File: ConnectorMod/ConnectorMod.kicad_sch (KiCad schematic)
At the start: 82 parts, among them J1 PJ-325, J10 VIN, J11 VCC, J12 MRX, J13 MTX, J14 DACL, J15 DACR, J16 DACG, J17 VSW, J2 PJ-325, J3 PJ-325, J4 PJ-066A, J5 BAT1, J6 BAT2, J7 AMP, J8 GNDA, J9 GND, Q1 MMBT3904, Q2 MMBT3904, Q3 MMBT3906, U1 TLP2366, U2 74LVC1G08, U3 TLV2372

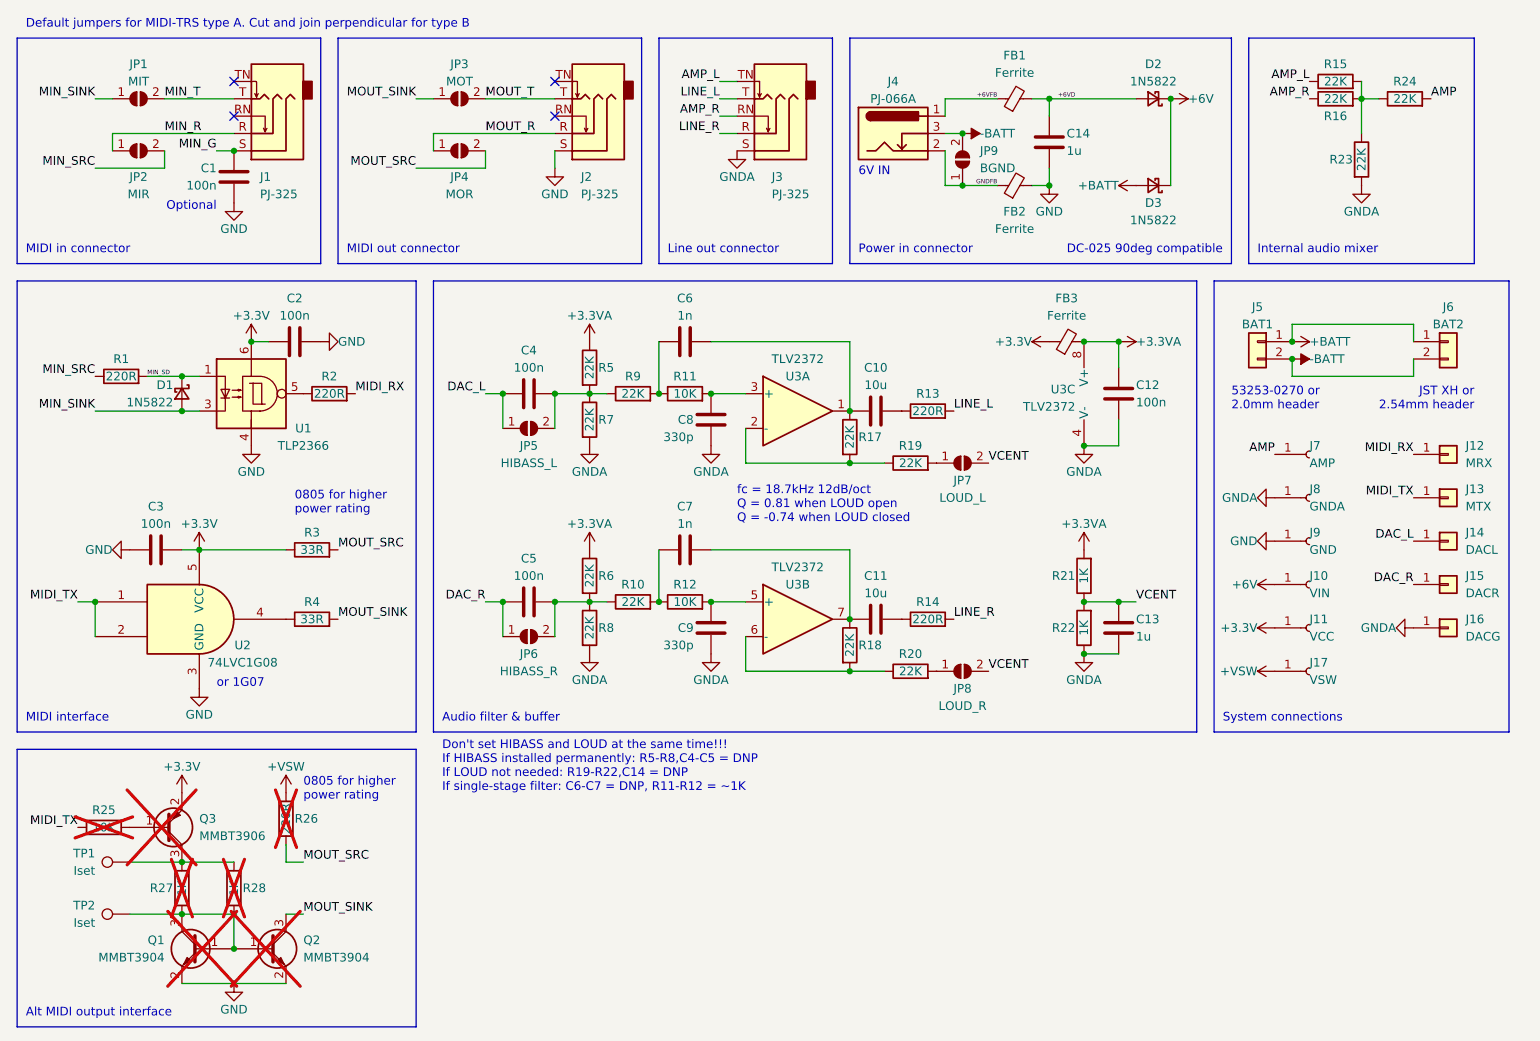
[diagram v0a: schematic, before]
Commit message: Remove loud jumper and tweak filter values
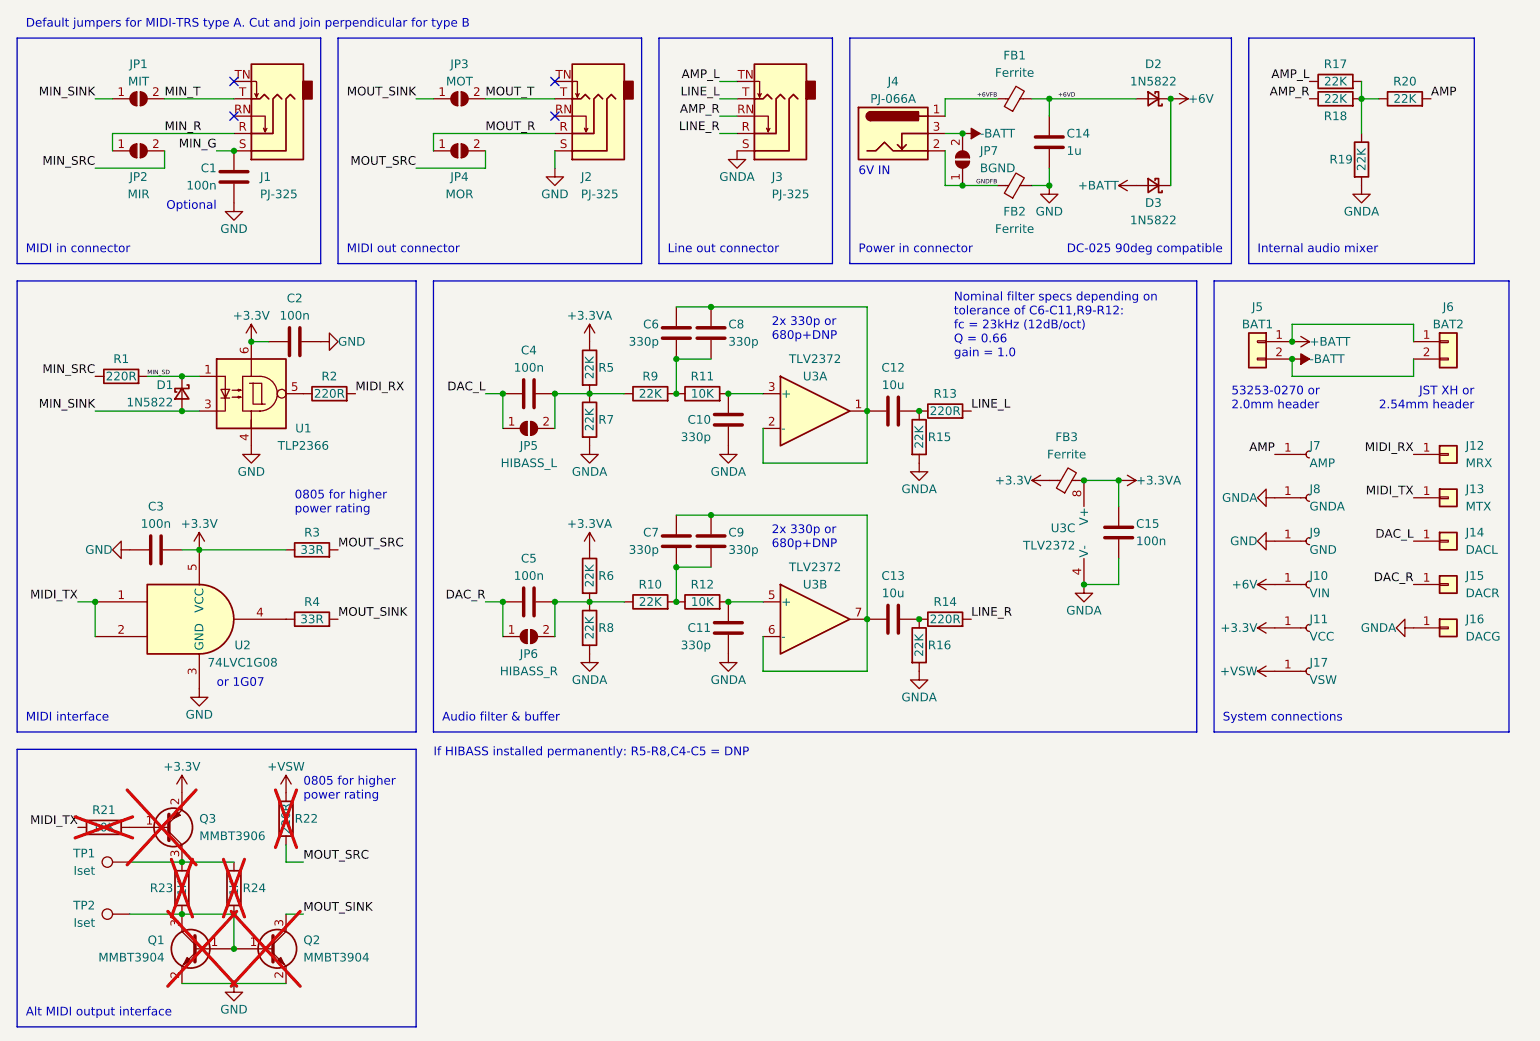
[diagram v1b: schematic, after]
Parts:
- removed C13: 1u, Capacitor_SMD:C_0805_2012Metric, symbol Device:C
- removed JP7: LOUD_L, project-parts:SolderJumper_Custom, symbol Jumper:SolderJumper_2_Open
- removed JP8: LOUD_R, project-parts:SolderJumper_Custom, symbol Jumper:SolderJumper_2_Open
- removed R19, R20: 22K, Resistor_SMD:R_0603_1608Metric, symbol Device:R
- removed R21, R22: 1K, Resistor_SMD:R_0603_1608Metric, symbol Device:R
- added C8, C9: 330p, Capacitor_SMD:C_0603_1608Metric, symbol Device:C
- C6, C7: value 1n -> 330p
- renumbered C8 to C10, C9 to C11, C10 to C12, C11 to C13, C12 to C15, JP9 to JP7, R17 to R15, R18 to R16, R15 to R17, R16 to R18, R23 to R19, R24 to R20, R25 to R21, R26 to R22, R27 to R23, R28 to R24
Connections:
- net GNDA: now also R15.2, R16.2
- net at C12.2, R13.1: now also R15.1
- net at U3.2 (-): now also C12.1, C6.1, U3.1, C8.1; no longer R15.2
- net at C13.2, R14.1: now also R16.1
- net at C6.2, R11.1, R9.2: now also C8.2
- net at U3.6 (-): now also C13.1, C7.1, U3.7, C9.1; no longer R16.2
- net at C7.2, R10.2, R12.1: now also C9.2
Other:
- note added: "2x 330p or 680p+DNP"
- note added: "If HIBASS installed permanently: R5-R8,C4-C5 = DNP"
- note added: "Nominal filter specs depending on tolerance of C6-C11,R9-R12: fc = 23kHz (12dB/oct) Q = 0.66 gain = 1.0"
- note removed: "Don't set HIBASS and LOUD at the same time!!! If HIBASS installed permanently: R5-R8,C4-C5 = DNP If LOUD not needed: R19-R22,C14 = DNP If single-stage filter: C6-C7 = DNP, R11-R12 = ~1K"
- note removed: "fc = 18.7kHz 12dB/oct Q = 0.81 when LOUD open Q = -0.74 when LOUD closed"
- moved on the sheet: C10, C11, C12, C13, C15, C6, C7, FB3, R10, R11, R12, R13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

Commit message: Change MIDI type jumpers to cross pads
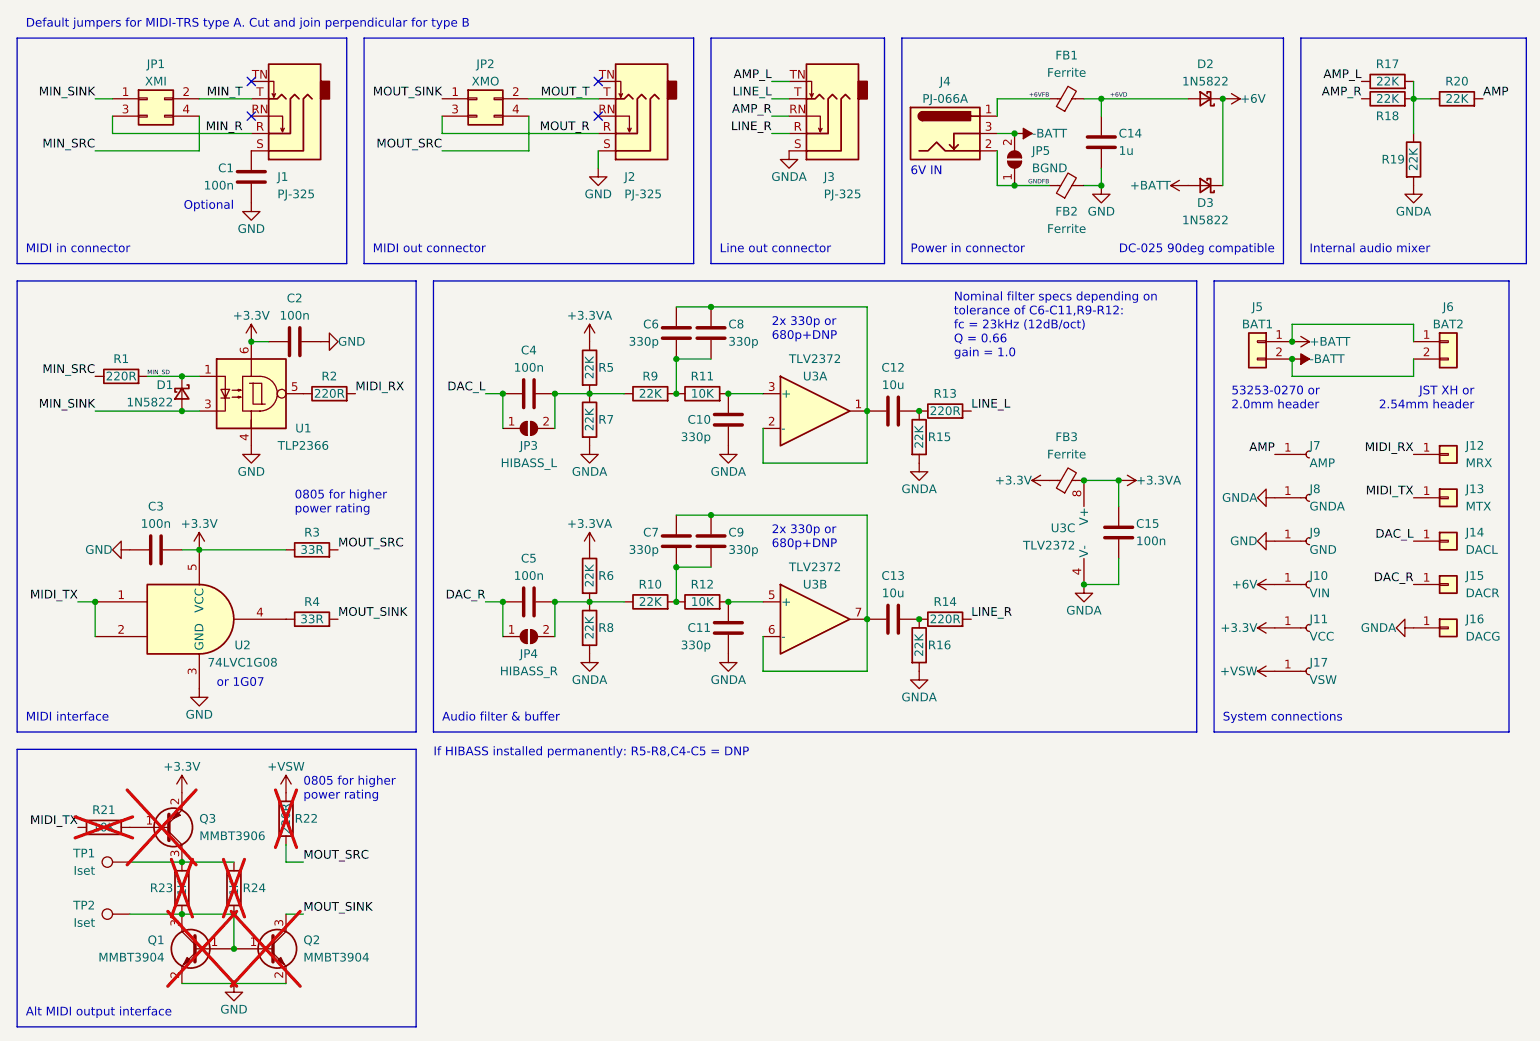
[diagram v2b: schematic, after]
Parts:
- removed JP1: MIT, project-parts:SolderJumper_Custom, symbol Jumper:SolderJumper_2_Open
- removed JP2: MIR, project-parts:SolderJumper_Custom, symbol Jumper:SolderJumper_2_Open
- removed JP3: MOT, project-parts:SolderJumper_Custom, symbol Jumper:SolderJumper_2_Open
- removed JP4: MOR, project-parts:SolderJumper_Custom, symbol Jumper:SolderJumper_2_Open
- added JP1: XMI, project-parts:SolderJumper_Cross, symbol Connector_Generic:Conn_02x02_Odd_Even
- added JP2: XMO, project-parts:SolderJumper_Cross, symbol Connector_Generic:Conn_02x02_Odd_Even
- renumbered JP5 to JP3, JP6 to JP4, JP7 to JP5
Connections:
- net MIN_R: now also JP1.3 (Pin_3)
- net MIN_SINK: now also JP1.1 (Pin_1)
- net MIN_SRC: now also JP1.4 (Pin_4)
- net MIN_T: now also JP1.2 (Pin_2)
- net MOUT_R: now also JP2.3 (Pin_3)
- net MOUT_SINK: now also JP2.1 (Pin_1)
- net MOUT_SRC: now also JP2.4 (Pin_4)
- net MOUT_T: now also JP2.2 (Pin_2)
- net MIN_G: no longer names the net of C1.1, J1.S
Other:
- moved on the sheet: C1, C14, D2, D3, FB1, FB2, J1, J2, J3, J4, JP5, R17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

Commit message: Use protected source/sink for MIDI out
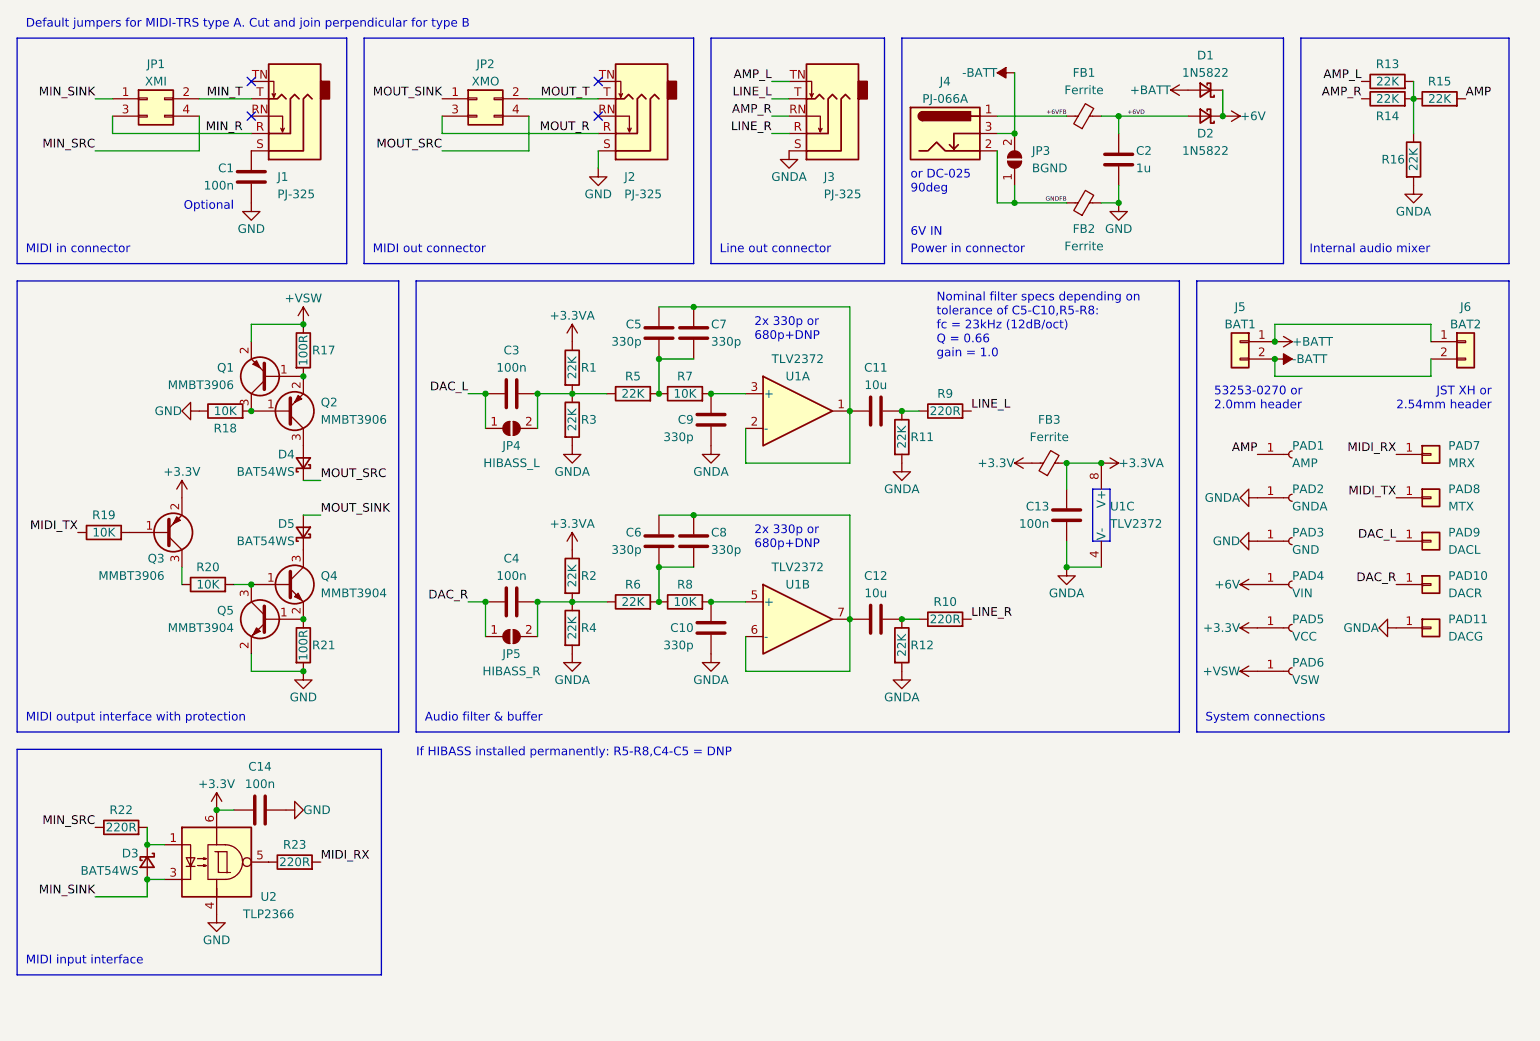
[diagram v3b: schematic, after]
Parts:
- removed C3: 100n, Capacitor_SMD:C_0603_1608Metric, symbol Device:C
- removed D1: 1N5822, Diode_SMD:D_SMA, symbol Device:D_Schottky_Small
- removed R1: 220R, Resistor_SMD:R_0805_2012Metric, symbol Device:R
- removed R23: 1K, Resistor_SMD:R_0603_1608Metric, symbol Device:R
- removed R3, R4: 33R, Resistor_SMD:R_0805_2012Metric, symbol Device:R
- removed TP1, TP2: Iset, TestPoint:TestPoint_Pad_1.5x1.5mm, symbol Connector:TestPoint
- removed U2: 74LVC1G08, Package_TO_SOT_SMD:SOT-23-5, symbol 74xGxx:74LVC1G08
- added D3, D4, D5: BAT54WS, Diode_SMD:D_SOD-323, symbol Device:D_Schottky_Small
- added Q2, Q3: MMBT3906, Package_TO_SOT_SMD:SOT-23, symbol Transistor_BJT:MMBT3906
- added R17: 100R, Resistor_SMD:R_0603_1608Metric, symbol Device:R
- added R18, R20: 10K, Resistor_SMD:R_0603_1608Metric, symbol Device:R
- Q1: renamed from Q3; now fitted; now in the parts list
- Q4: renamed from Q2; now fitted; now in the parts list
- Q5: renamed from Q1; now fitted; now in the parts list
- R19: renamed from R21; now fitted; now in the parts list
- R21: renamed from R24; value 1K -> 100R; now fitted; now in the parts list
- R22: footprint Resistor_SMD:R_0805_2012Metric -> Resistor_SMD:R_0603_1608Metric; now fitted; now in the parts list
- U2: renamed from U1; footprint Package_SO:SO-6_4.4x3.6mm_P1.27mm -> Package_SO:SO-5_4.4x3.6mm_P1.27mm
- renumbered C11 to C10, C12 to C11, C13 to C12, C15 to C13, C2 to C14, C14 to C2, C4 to C3, C5 to C4, C6 to C5, C7 to C6, C8 to C7, C9 to C8, C10 to C9, D3 to D1, JP5 to JP3, JP3 to JP4, JP4 to JP5, J7 to PAD1, J15 to PAD10, J16 to PAD11, J8 to PAD2, J9 to PAD3, J10 to PAD4, J11 to PAD5, J17 to PAD6, J12 to PAD7, J13 to PAD8, J14 to PAD9, R5 to R1, R14 to R10, R15 to R11, R16 to R12, R17 to R13, R18 to R14, R20 to R15, R19 to R16, R6 to R2, R2 to R23, R7 to R3, R8 to R4, R9 to R5, R10 to R6, R11 to R7, R12 to R8, R13 to R9, U3 to U1
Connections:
- net +3.3V: now also Q3.2 (E); no longer Q1.2 (E)
- net +VSW: now also Q1.2 (E), R17.1; no longer R22.1
- net GND: now also R21.2, R18.1; no longer Q4.2 (E)
- net MIN_SINK: now also D3.2 (A)
- net MIN_SRC: now also R22.1
- net MOUT_SINK: now also D5.2 (A); no longer Q4.3 (C)
- net MOUT_SRC: now also D4.1 (K); no longer R22.2
- net at Q4.1 (B), Q5.3 (C): now also R20.2; no longer Q5.1 (B), R21.2
- net at Q1.3 (C): now also Q2.1 (B), R18.2; no longer R21.1
- net at R19.2: now also Q3.1 (B); no longer Q1.1 (B)
- net MIN_SD: no longer names the net of U2.1
- net MIN_SD: now also R22.2, D3.1 (K)
- new net: D5.1 (K), Q4.3 (C)
- new net: Q3.3 (C), R20.1
- new net: D4.2 (A), Q2.3 (C)
- new net: Q1.1 (B), Q2.2 (E), R17.2
- new net: Q4.2 (E), Q5.1 (B), R21.1
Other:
- note added: "MIDI input interface"
- note added: "MIDI output interface with protection"
- note added: "Nominal filter specs depending on tolerance of C5-C10,R5-R8: fc = 23kHz (12dB/oct) Q = 0.66 gain = 1.0"
- note added: "or DC-025 90deg"
- note removed: "0805 for higher power rating"
- note removed: "Alt MIDI output interface"
- note removed: "DC-025 90deg compatible"
- note removed: "MIDI interface"
- note removed: "Nominal filter specs depending on tolerance of C6-C11,R9-R12: fc = 23kHz (12dB/oct) Q = 0.66 gain = 1.0"
- note removed: "or 1G07"
- moved on the sheet: C10, C11, C12, C13, C14, C2, C3, C4, C5, C6, C7, C8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
